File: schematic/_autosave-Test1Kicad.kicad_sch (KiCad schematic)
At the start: 20 parts, among them IC1 BMI055, U1 STM32F765IIKx, U2 NEO-M8N, U3 IST8310, U4 ICM-20602, U5 ICM-20689, U6 MS5611-01BA

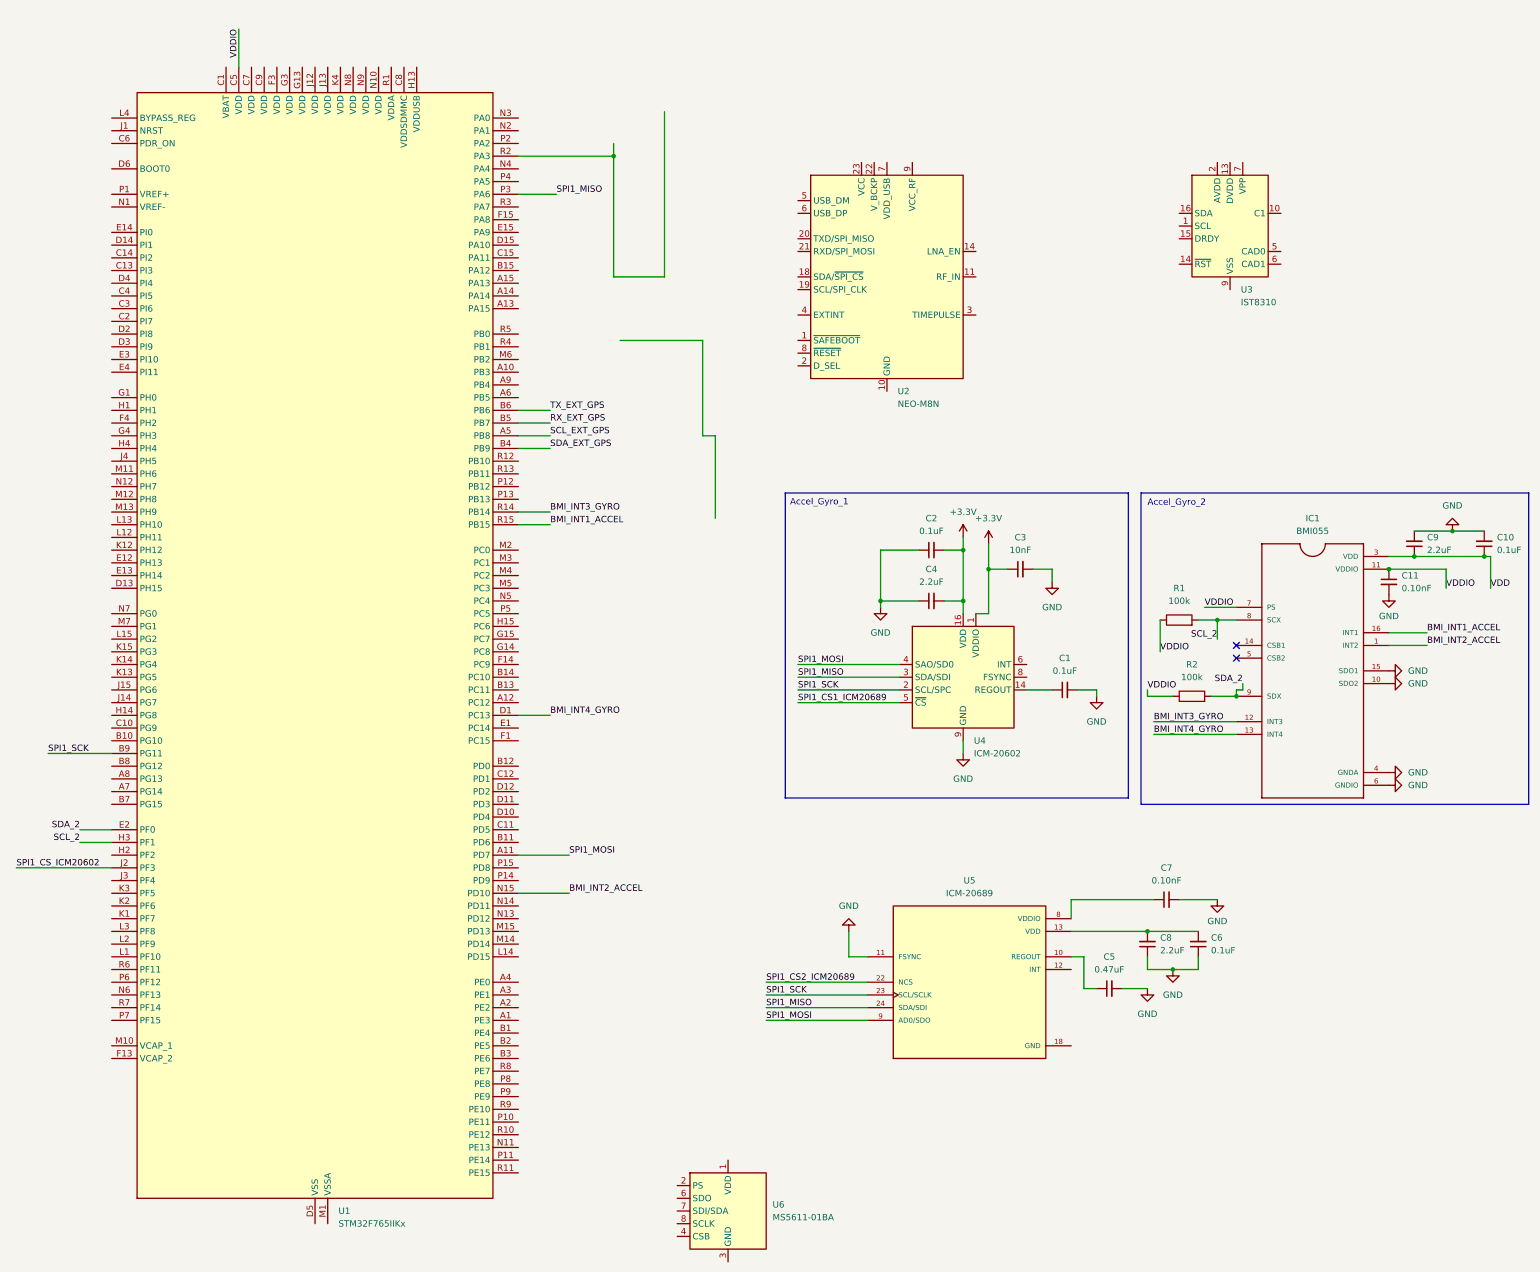
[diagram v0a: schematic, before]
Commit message: IST8310
finished the IST and fixed a few issues with the BMI
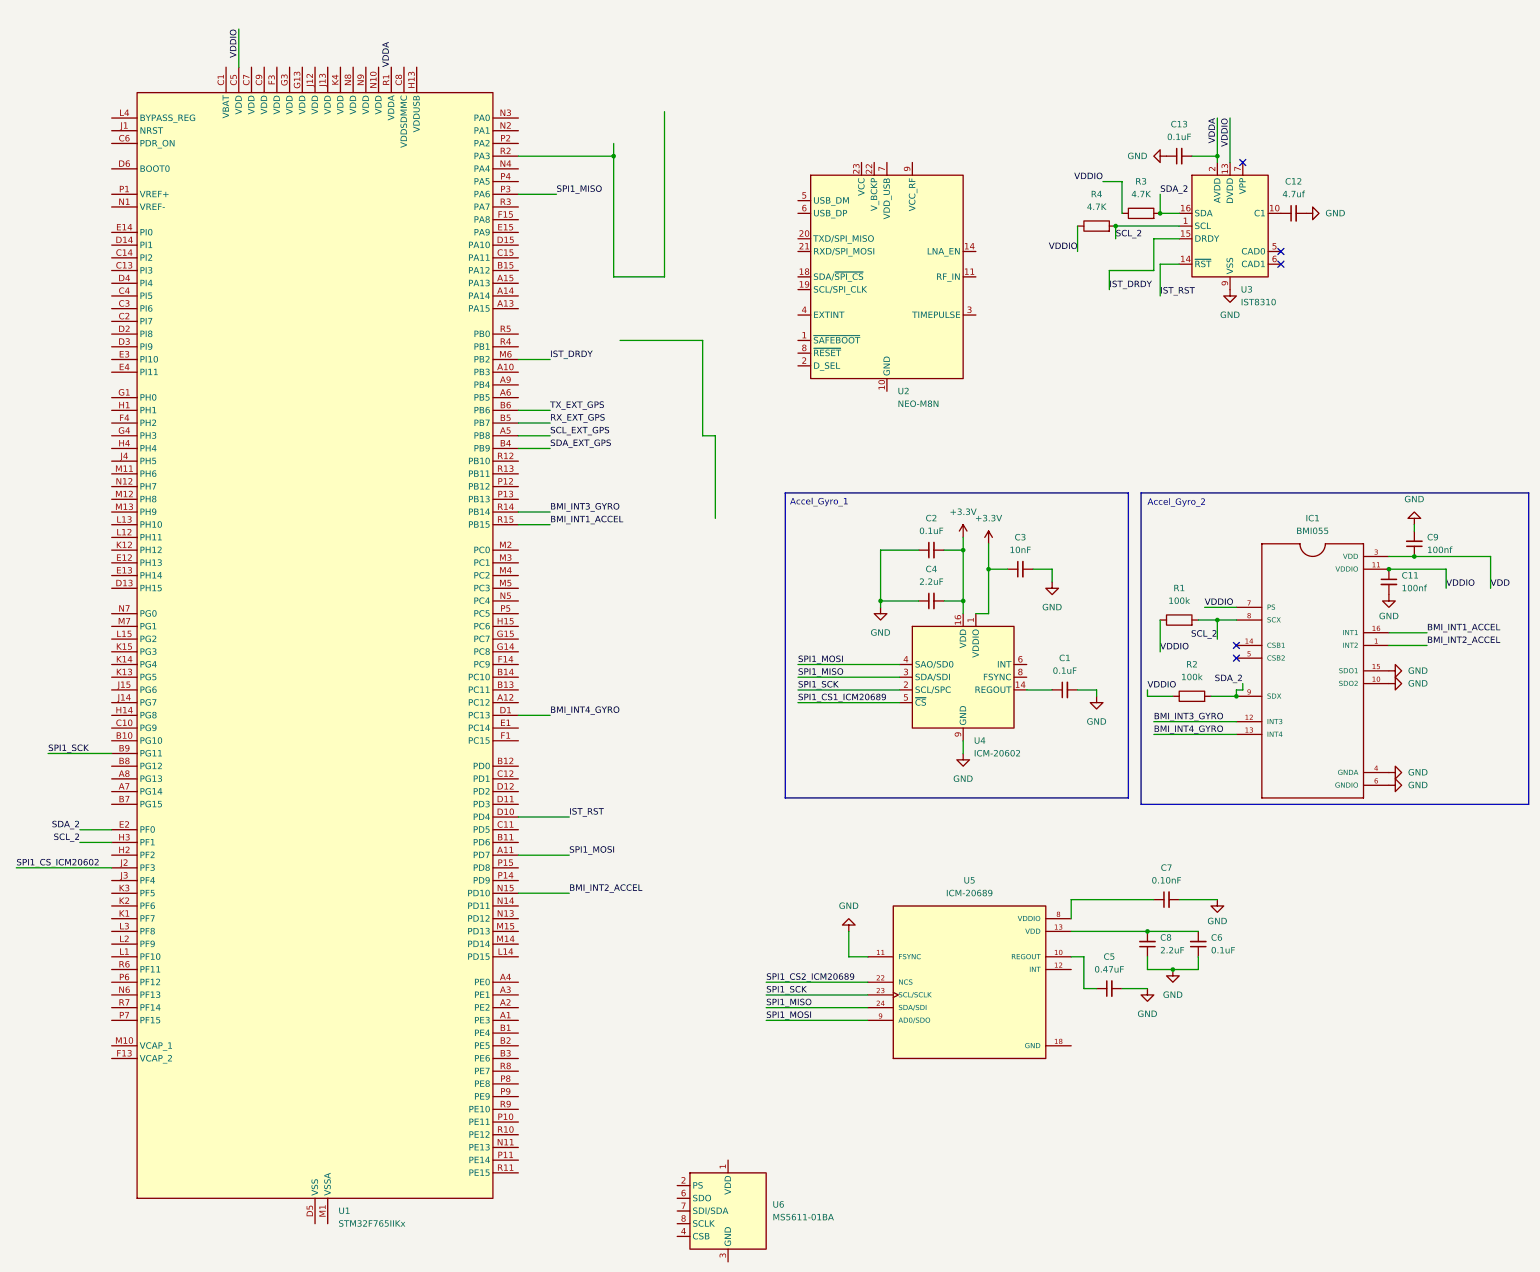
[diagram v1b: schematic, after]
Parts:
- removed C10: 0.1uF, symbol Device:C_Small
- added C12: 4.7uf, symbol Device:C_Small
- added C13: 0.1uF, symbol Device:C_Small
- added R3, R4: 4.7K, symbol Device:R
- C11: value 0.10nF -> 100nf
- C9: value 2.2uF -> 100nf
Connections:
- net GND: now also U3.11 (VSS), U3.9 (VSS), C12.2, C13.1
- net SCL_2: now also U3.1 (SCL), R4.2
- net SDA_2: now also U3.16 (SDA), R3.2
- net VDDIO: now also U3.13 (DVDD), R3.1, R4.1
- net IST_RST: now reaches U1.D10 (PD4)
- net IST_RST: now also U3.14 (~{RST})
- net IST_DRDY: now reaches U1.M6 (PB2)
- net IST_DRDY: now also U3.15 (DRDY)
- net VDDA: now reaches U1.R1 (VDDA)
- net VDDA: now also U3.2 (AVDD), C13.2
- net at U3.10 (C1): now also C12.1
- no-connect marks 2 -> 5

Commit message: Minnor Update
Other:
- note added: "Magnetometer"
- moved on the sheet: C12, C13, R3, R4, U3

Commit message: ICM20689(1)
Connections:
- net SPI1_CS2_ICM20689 is gone; now on net SPI1_CS1_ICM20689: U5.22 (NCS)
- net GND: now also U5.18 (GND)
- net SPI1_CS1_ICM20689: now also U1.H2 (PF2); no longer U4.5 (~{CS})
- net SPI1_DRDY1_ICM20689: now reaches U1.A9 (PB4)
- net SPI1_DRDY1_ICM20689: now also U5.12 (INT)
- net SPI4_CS1_MS5611: now reaches U1.L1 (PF10)
- net SPI4_CS1_MS5611: now also U6.4 (CSB), U6.5 (CSB)
- net SPI1_CS_ICM20602 renamed SPI1_CS2_ICM20602
- net SPI1_CS2_ICM20602: now also U4.5 (~{CS})
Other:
- moved on the sheet: C7

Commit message: Barometer,Oscillator
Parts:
- added C10: 100nF, symbol Device:C_Small
- added C14, C15: 22pF, symbol Device:C_Small
- added Y1: ABM2-8.000MHZ-D4Y-T, ABM2-8.000MHZ-D4Y-T:XTAL_ABM2-8.000MHZ-D4Y-T, symbol ABM2-8.000MHZ-D4Y-T:ABM2-8.000MHZ-D4Y-T
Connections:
- net GND: now also U6.2 (PS), U6.3 (GND), C10.1, C14.2, C15.1
- net VDD: now also C2.2, C4.2, C6.2, C8.2, U1.C7 (VDD), U4.16 (VDD), U5.13 (VDD), U6.1 (VDD), C10.2
- net VDDIO: now also C3.1, C7.1, U4.1 (VDDIO), U5.8 (VDDIO)
- net SPI4_SCK: now reaches U1.A2 (PE2)
- net SPI4_SCK: now also U6.8 (SCLK)
- net SPI4_MOSI: now reaches U1.B3 (PE6)
- net SPI4_MOSI: now also U6.7 (SDI/SDA)
- net OSC_IN: now reaches U1.G1 (PH0)
- net OSC_IN: now also C15.2, Y1.1
- net OSC_OUT: now reaches U1.H1 (PH1)
- net OSC_OUT: now also C14.1, Y1.2
- net SPI4_MISO: now reaches U1.N11 (PE13)
- net SPI4_MISO: now also U6.6 (SDO)
- removed net +3.3V: C2.2, C3.1, C4.2, U4.1 (VDDIO), U4.16 (VDD)
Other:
- moved on the sheet: C3, C5, C6, C7, C8, U2, U5, U6
